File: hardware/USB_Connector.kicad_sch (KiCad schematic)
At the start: 5 parts, among them J1 USB4105-GF-A, U6 USBLC6-2SC6

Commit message: encore plein de truc chouette
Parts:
- added C1: 100nF, symbol Device:C
- added D2, D3: 3.3v, symbol Device:D_Zener
- added R1: 1M, symbol Device:R
- added R11, R12: 100, symbol Device:R
- added TP10: GND, symbol Connector:TestPoint
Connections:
- net CC1: now also R11.1
- net CC2: now also R12.1
- net GND: now also C1.1, D2.2 (A), D3.2 (A), R1.1, TP10.1
- net SHELL_GND: now also C1.2, R1.2
- new net CC1_ADC: D3.1 (K), R11.2
- new net CC2_ADC: D2.1 (K), R12.2

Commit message: Encore plein de truc chouette
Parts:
- added TP19: D+, symbol Connector:TestPoint
- added TP20: D-, symbol Connector:TestPoint
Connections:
- net D+: now also TP19.1
- net D-: now also TP20.1
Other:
- company: Lang & Hiltpold SNC -> Lang & Hiltpold Software SNC
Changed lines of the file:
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@@
 		(title "STM32-DevBoard")
 		(date "2026-06-03")
-		(company "Lang & Hiltpold SNC")
+		(company "Lang & Hiltpold Software SNC")
 	)
 	(junction
@@
 	)
 	(junction
+		(at 209.55 96.52)
+		(diameter 0)
+		(color 0 0 0 0)
+	)
+	(junction
 		(at 135.89 87.63)
 		(diameter 0)
@@
 		(color 0 0 0 0)
 	)
+	(junction
+		(at 209.55 93.98)
+		(diameter 0)
+		(color 0 0 0 0)
+	)
 	(no_connect
 		(at 132.08 100.33)
@@
 	(wire
 		(pts
+			(xy 224.79 88.9) (xy 224.79 93.98)
+		)
+		(stroke
+			(width 0)
+			(type default)
+		)
+	)
+	(wire
+		(pts
 			(xy 35.56 129.54) (xy 35.56 130.81)
 		)
@@
 	(wire
 		(pts
+			(xy 209.55 96.52) (xy 209.55 97.79)
+		)
+		(stroke
+			(width 0)
+			(type default)
+		)
+	)
+	(wire
+		(pts
 			(xy 110.49 138.43) (xy 110.49 140.97)
 		)
@@
 	(wire
 		(pts
+			(xy 209.55 92.71) (xy 209.55 93.98)
+		)
+		(stroke
+			(width 0)
+			(type default)
+		)
+	)
+	(wire
+		(pts
 			(xy 233.68 39.37) (xy 233.68 49.53)
 		)
@@
 	(wire
 		(pts
+			(xy 240.03 96.52) (xy 209.55 96.52)
+		)
+		(stroke
+			(width 0)
+			(type default)
+		)
+	)
+	(wire
+		(pts
 			(xy 135.89 87.63) (xy 132.08 87.63)
 		)
@@
 	(wire
 		(pts
+			(xy 240.03 88.9) (xy 240.03 96.52)
+		)
+		(stroke
+			(width 0)
+			(type default)
+		)
+	)
+	(wire
+		(pts
 			(xy 132.08 92.71) (xy 139.7 92.71)
 		)
@@
 		(pts
 			(xy 132.08 105.41) (xy 146.05 105.41)
+		)
+		(stroke
+			(width 0)
+			(type default)
+		)
+	)
+	(wire
+		(pts
+			(xy 209.55 93.98) (xy 224.79 93.98)
 		)
 		(stroke
@@
 	(hierarchical_label "D+"
 		(shape bidirectional)
-		(at 209.55 93.98 0)
+		(at 209.55 92.71 90)
 		(effects
 			(font
@@
 	(hierarchical_label "D-"
 		(shape bidirectional)
-		(at 209.55 96.52 0)
-		(effects
-			(font
-				(size 1.27 1.27)
-			)
-			(justify left)
+		(at 209.55 97.79 270)
+		(effects
+			(font
+				(size 1.27 1.27)
+			)
+			(justify right)
 		)
 	)
@@
 			)
 			(justify left)
+		)
+	)
+	(symbol
+		(lib_id "Connector:TestPoint")
+		(at 224.79 88.9 0)
+		(unit 1)
+		(body_style 1)
+		(exclude_from_sim no)
+		(in_bom yes)
+		(on_board yes)
+		(in_pos_files yes)
+		(dnp no)
+		(fields_autoplaced yes)
+		(property "Reference" "TP19"
+			(at 227.33 84.3279 0)
+			(show_name no)
+			(do_not_autoplace no)
+			(effects
+				(font
+					(size 1.27 1.27)
+				)
+				(justify left)
+			)
+		)
+		(property "Value" "D+"
+			(at 227.33 86.8679 0)
+			(show_name no)
+			(do_not_autoplace no)
+			(effects
+				(font
+					(size 1.27 1.27)
+				)
+				(justify left)
+			)
+		)
+		(property "Footprint" ""
+			(at 229.87 88.9 0)
+			(hide yes)
+			(show_name no)
+			(do_not_autoplace no)
+			(effects
+				(font
+					(size 1.27 1.27)
+				)
+			)
+		)
+		(property "Datasheet" ""
+			(at 229.87 88.9 0)
+			(hide yes)
+			(show_name no)
+			(do_not_autoplace no)
+			(effects
+				(font
+					(size 1.27 1.27)
+				)
+			)
+		)
+		(property "Description" "test point"
+			(at 224.79 88.9 0)
+			(hide yes)
+			(show_name no)
+			(do_not_autoplace no)
+			(effects
+				(font
+					(size 1.27 1.27)
+				)
+			)
+		)
+		(pin "1"
+		)
+		(instances
+			(project "STM32_DevBoard"
+				(path "/1ce911dd-e46b-4dca-9b0b-c360e42c38af/94c743bf-3100-466e-980d-6fa8a14eeb79"
+					(reference "TP19")
+					(unit 1)
+				)
+			)
 		)
 	)
@@
 					(unit 1)
 				)
+			)
+		)
+	)
+	(symbol
+		(lib_id "Connector:TestPoint")
+		(at 240.03 88.9 0)
+		(unit 1)
+		(body_style 1)
+		(exclude_from_sim no)
+		(in_bom yes)
+		(on_board yes)
+		(in_pos_files yes)
+		(dnp no)
+		(fields_autoplaced yes)
+		(property "Reference" "TP20"
+			(at 242.57 84.3279 0)
+			(show_name no)
+			(do_not_autoplace no)
+			(effects
+				(font
+					(size 1.27 1.27)
+				)
+				(justify left)
+			)
+		)
+		(property "Value" "D-"
+			(at 242.57 86.8679 0)
+			(show_name no)
+			(do_not_autoplace no)
+			(effects
+				(font
+					(size 1.27 1.27)
+				)
+				(justify left)
+			)
+		)
+		(property "Footprint" ""
+			(at 245.11 88.9 0)
+			(hide yes)
+			(show_name no)
+			(do_not_autoplace no)
+			(effects
+				(font
+					(size 1.27 1.27)
+				)
+			)
+		)
+		(property "Datasheet" ""
+			(at 245.11 88.9 0)
+			(hide yes)
+			(show_name no)
+			(do_not_autoplace no)
+			(effects
+				(font
+					(size 1.27 1.27)
+				)
+			)
+		)
+		(property "Description" "test point"
+			(at 240.03 88.9 0)
+			(hide yes)
+			(show_name no)
+			(do_not_autoplace no)
+			(effects
+				(font
+					(size 1.27 1.27)
+				)
+			)
+		)
+		(pin "1"
+		)
+		(instances
+			(project "STM32_DevBoard"
+				(path "/1ce911dd-e46b-4dca-9b0b-c360e42c38af/94c743bf-3100-466e-980d-6fa8a14eeb79"
+					(reference "TP20")
+					(unit 1)
+				)

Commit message: Schema termine ?
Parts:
- added R14, R15: 22, symbol Device:R
- renumbered C1 to C5, C10 to C6, R2 to R10, R3 to R11, R11 to R12, R12 to R13, R1 to R9, TP20 to TP10, TP10 to TP8, TP19 to TP9, U6 to U3
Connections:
- net D+: now also R14.1; no longer TP9.1
- net D-: now also R15.1; no longer TP10.1
- new net: R14.2, TP9.1
- new net: R15.2, TP10.1
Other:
- moved on the sheet: TP10, TP9

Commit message: Assignation terminee
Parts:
- removed D2, D3: 3.3v, symbol Device:D_Zener
- added D2, D3: CC, Diode_SMD:D_SOD-323, symbol Device:D_Schottky
- C5, C6: footprint (none) -> Capacitor_SMD:C_0805_2012Metric
- R10, R11, R12, R13, R14, R15, R9: footprint (none) -> Resistor_SMD:R_0805_2012Metric
- TP10, TP8, TP9: footprint (none) -> TestPoint:TestPoint_Loop_D2.50mm_Drill1.0mm
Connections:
- net CC1_ADC: now also D2.2 (A)
- net CC2_ADC: now also D3.2 (A)
- net VBUS: now also D2.1 (K), D3.1 (K)

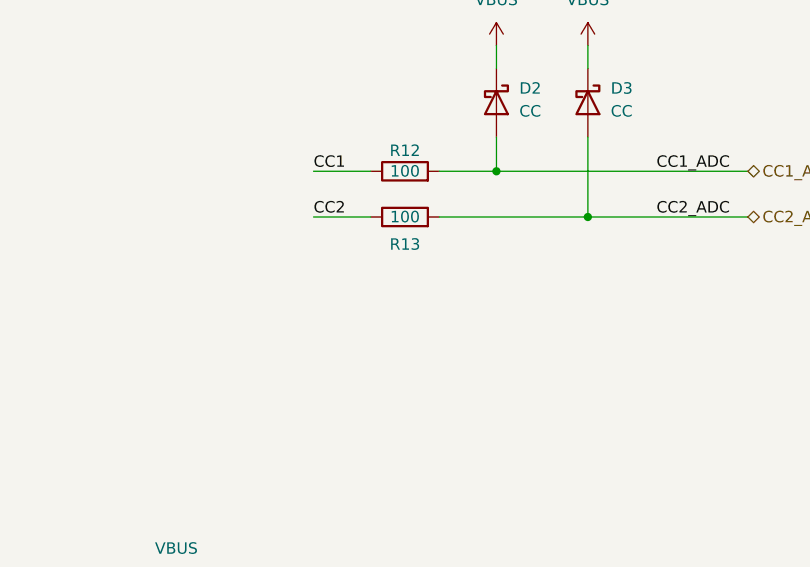
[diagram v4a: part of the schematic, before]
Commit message: USB connector CC Resistor not mount text added
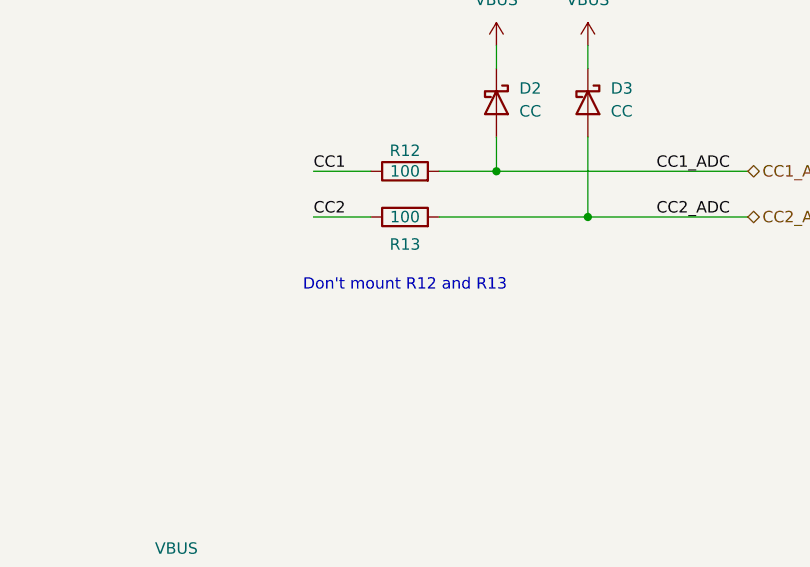
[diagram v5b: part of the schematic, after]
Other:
- note added: "Don't mount R12 and R13"
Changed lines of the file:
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@@
 		(company "Lang & Hiltpold Software SNC")
+	)
+	(text "Don't mount R12 and R13\n"
+		(exclude_from_sim no)
+		(at 214.63 52.07 0)
+		(effects
+			(font
+				(size 1.27 1.27)
+			)
+		)
 	)
 	(junction
